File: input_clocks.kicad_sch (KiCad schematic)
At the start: 86 parts, among them J201 REFIN, J202 REFIN_DIRECT_P, J203 REFIN_DIRECT_N, J208 VTUNE, T201 TC2-1T+, U203 TSV914, U204 74LVC1G66, X201 XTCLH40M000CHJA0P0

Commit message: Updated schematics
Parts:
- removed J?: TCXO_ON_LED, symbol Connector_Generic:Conn_01x02
- added D?: TCXO_ON, LED_SMD:LED_0603_1608Metric_Pad1.05x0.95mm_HandSolder, symbol Device:LED
- added FB?: TODO, Inductor_SMD:L_0603_1608Metric_Pad1.05x0.95mm_HandSolder, symbol Device:FerriteBead_Small
- added R? (x2): DNP, Resistor_SMD:R_0603_1608Metric_Pad0.98x0.95mm_HandSolder, symbol Device:R
- added R?: TODO, Resistor_SMD:R_0603_1608Metric_Pad0.98x0.95mm_HandSolder, symbol Device:R
- R?: value 470 -> 2k
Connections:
- net +5V: now also FB?.1; no longer C?.1, U?.2 (VIN)
- net CLKIN_0: now also R?.1
- net DUTY_OUT_N: now also D207.1 (K), D208.2 (A), R?.2
- net DUTY_OUT_P: now also R227.1, R?.2
- net GND: now also C?.1, R?.2; no longer C?.2
- net VCC_TCXO: now also D?.2 (A); no longer R?.2
- net Vctrl: now also R?.2; no longer C227.1, D?.3, J208.1 (In)
- net ~{CLKIN_0}: now also R?.1
- net at R?.1: now also D?.1 (K)
- net at D207.2 (A), D208.1 (K): now also R227.2
- new net: C227.1, D?.3, J208.1 (In), R?.1
- new net: C?.2, FB?.2, U?.2 (VIN)
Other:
- moved on the sheet: C205, C206, C216, C217, C218, C225, C226, C227, C228, C230, C232, C234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

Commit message: Finished schematics
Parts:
- added JP503: Jumper_2_Bridged, symbol Jumper:Jumper_2_Bridged
- gave numbers to parts that had none: 19
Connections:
- net VCC renamed VCC_fREF
- net VCC_fREF: now also JP503.1 (A); no longer U204.5 (VCC)
- new net: JP503.2 (B), U204.5
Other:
- company: (none) -> Petr Polasek
- title: (none) -> Generator 0.0125 - 6.4 GHz (0.02 - 9.8 GHz)
- moved on the sheet: C225, C226, C228, C232, C235, C501, C503, D207, D208, R227, R230, R231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

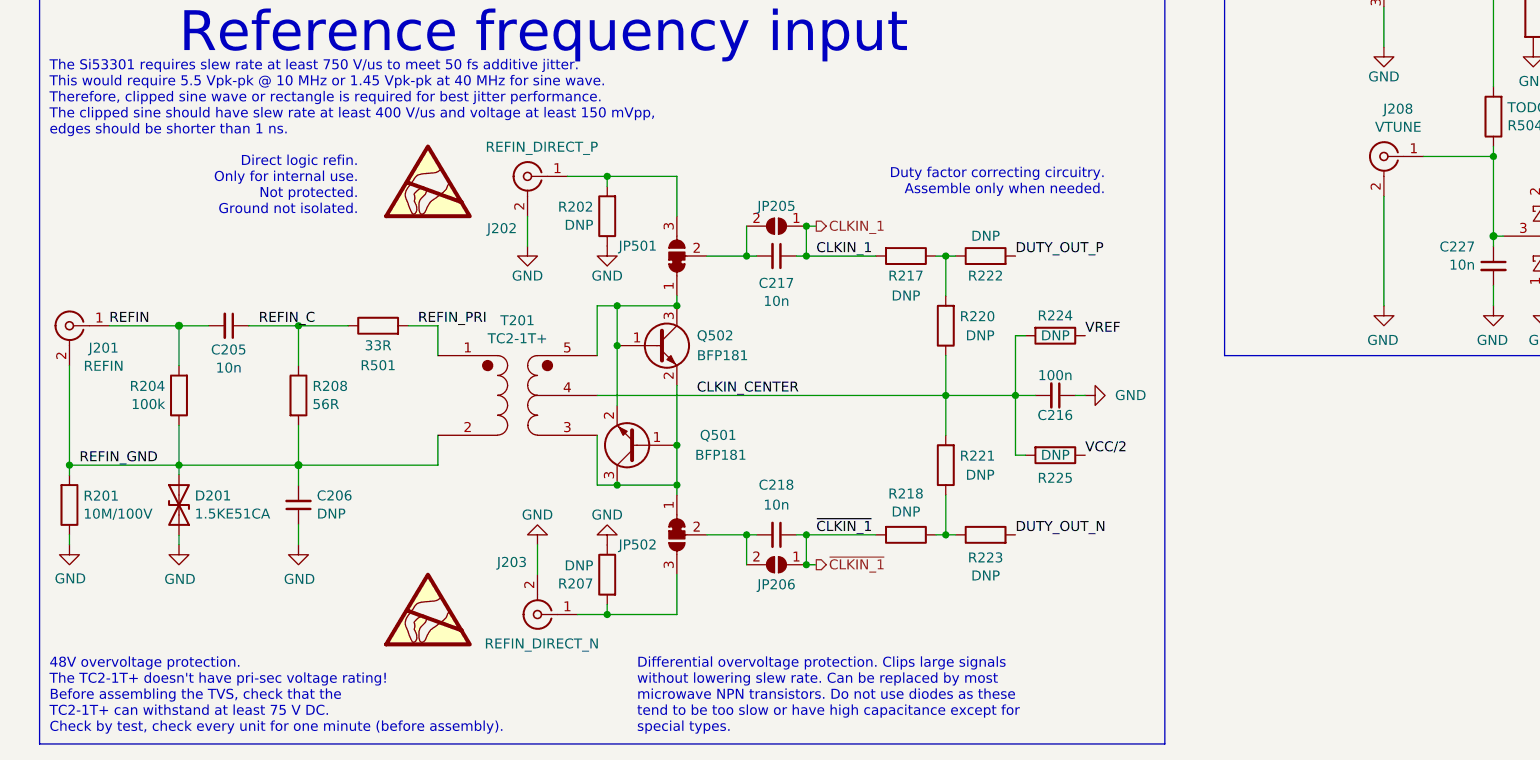
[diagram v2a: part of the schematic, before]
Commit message: Schematic fixes
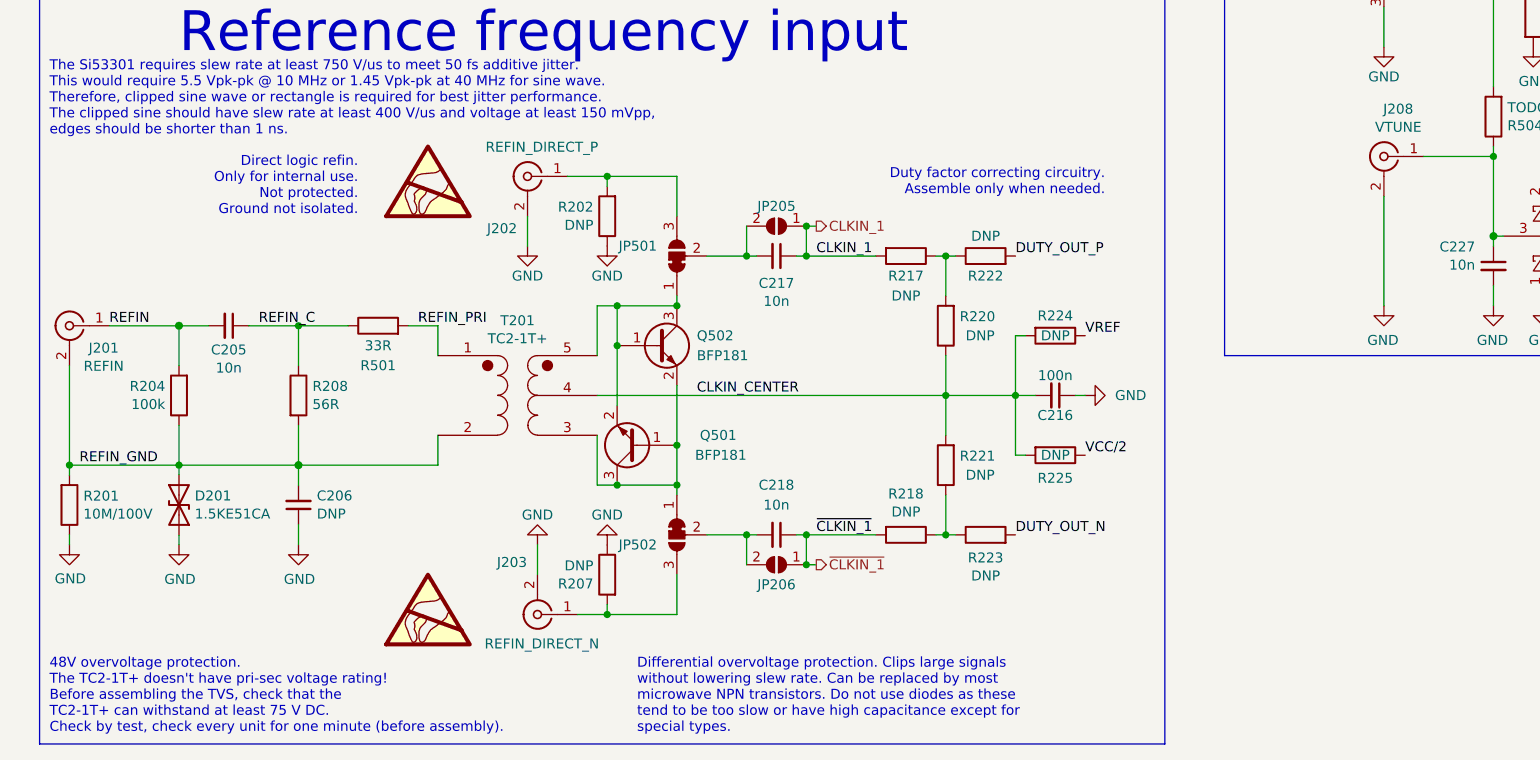
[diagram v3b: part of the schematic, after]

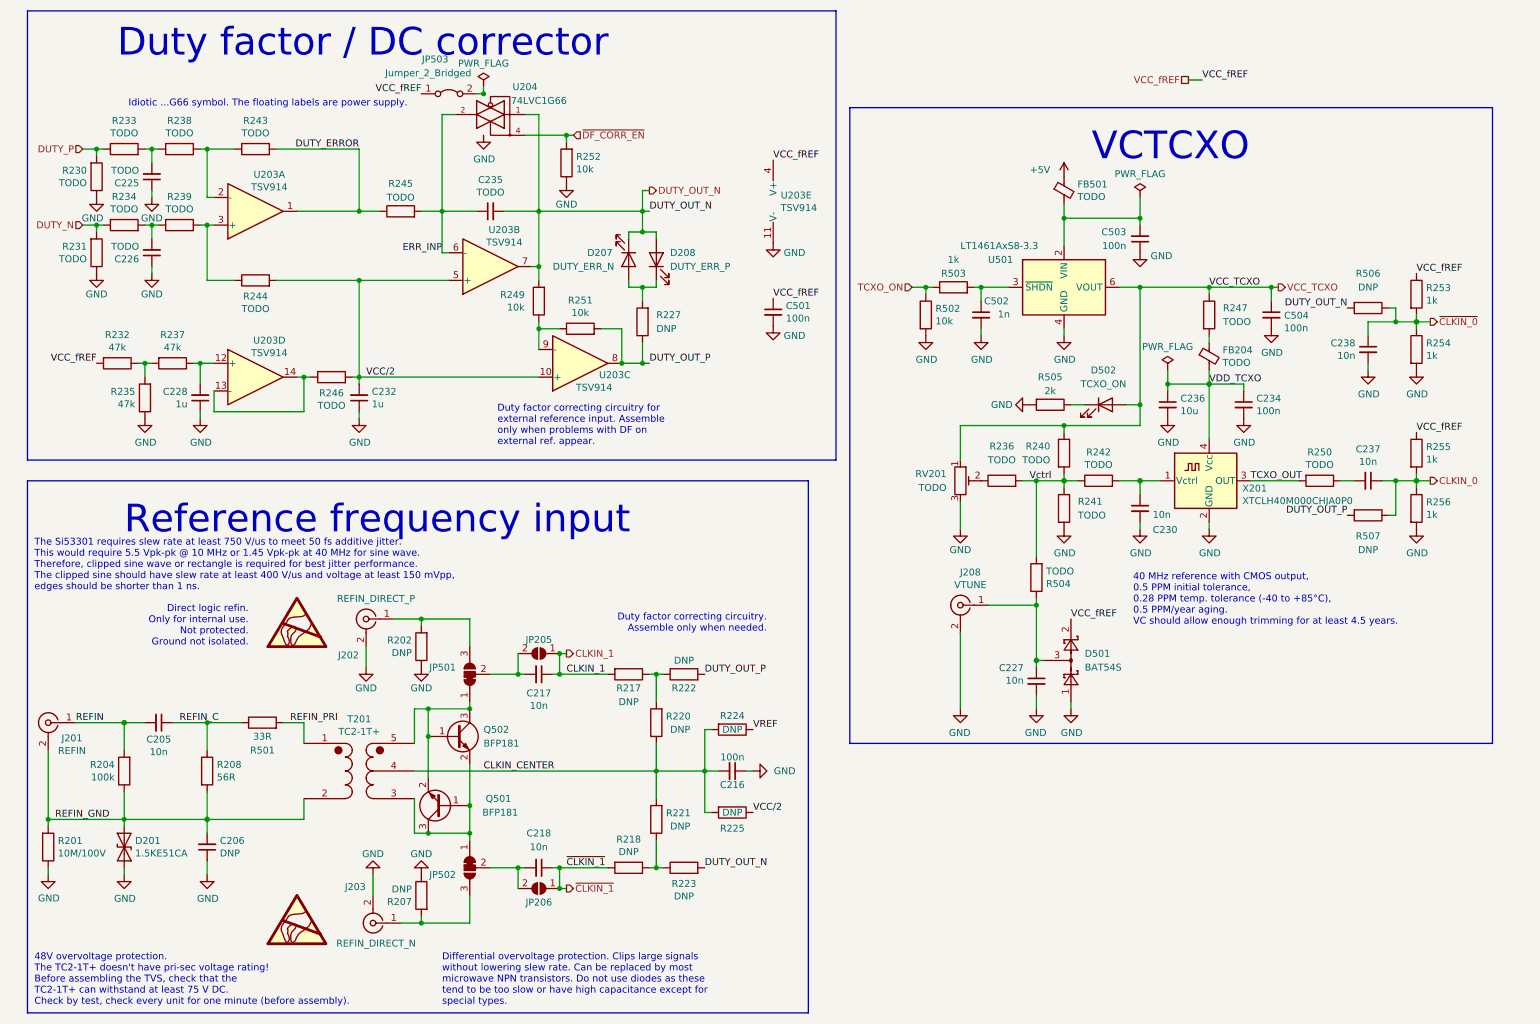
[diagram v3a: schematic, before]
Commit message: Schematic checked. All footprints assigned. Electrolytics need footprint check, so do the RS485 and power connectors and the MuRata oscillator (also it is now EOL) and the crystal. The power protection transils on aux input/output need replacement. PCB in sync with SCH.
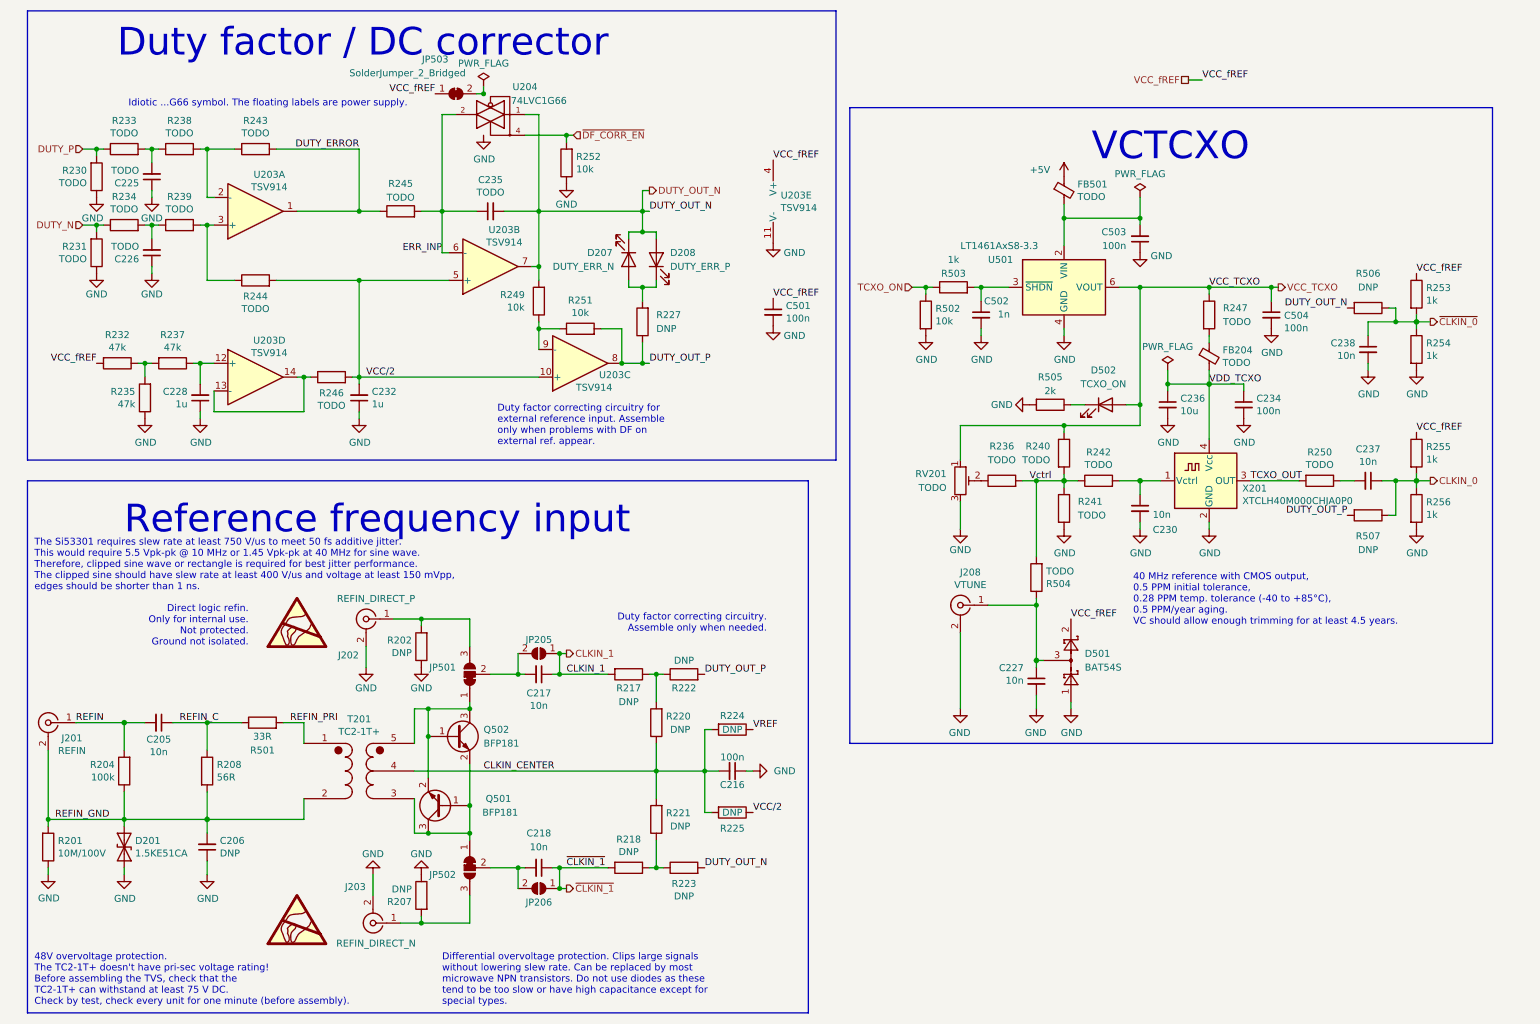
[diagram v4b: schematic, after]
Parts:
- removed JP503: Jumper_2_Bridged, symbol Jumper:Jumper_2_Bridged
- added JP503: SolderJumper_2_Bridged, Jumper:SolderJumper-2_P1.3mm_Bridged_RoundedPad1.0x1.5mm, symbol Jumper:SolderJumper_2_Bridged
- J202, J203, J208: footprint petr_kicad:SMA_rosenberger_hybrid -> Connector_Coaxial:U.FL_Molex_MCRF_73412-0110_Vertical
- JP501, JP502: footprint (none) -> Jumper:SolderJumper-3_P1.3mm_Bridged12_RoundedPad1.0x1.5mm_NumberLabels
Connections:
- net VCC_fREF: now also JP503.1 (A)
- net at U204.5: now also JP503.2 (B)

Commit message: Resolved all broken symbols / packages / links except TCXO.
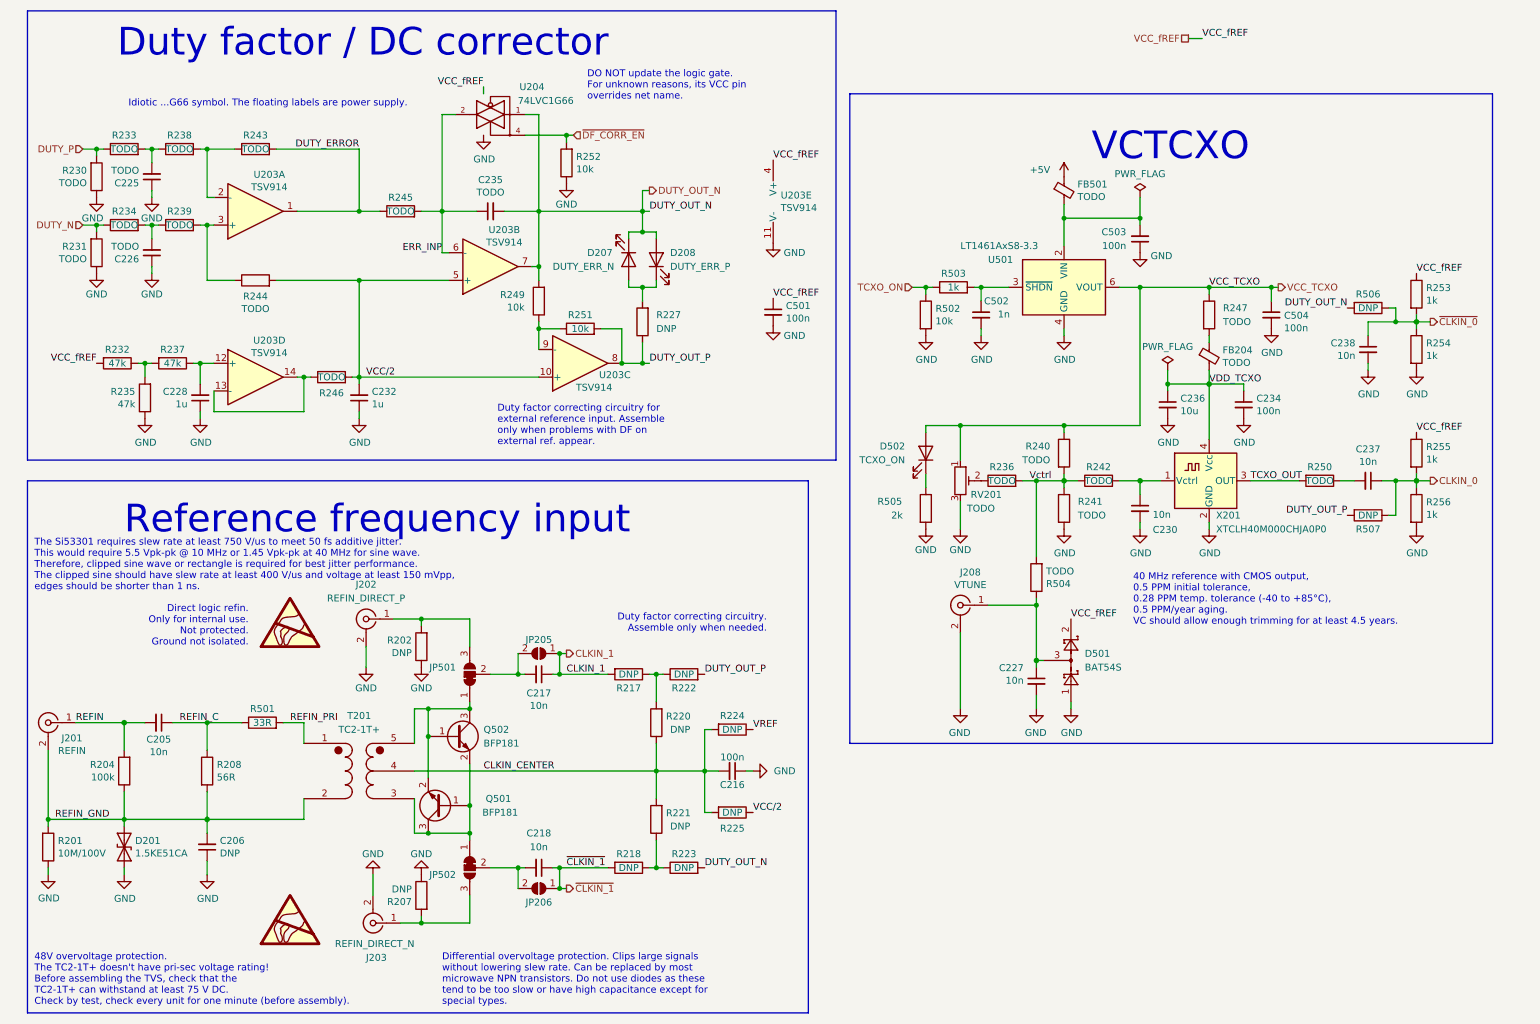
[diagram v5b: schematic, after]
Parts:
- removed J202: REFIN_DIRECT_P, Connector_Coaxial:U.FL_Molex_MCRF_73412-0110_Vertical, symbol Connector:Conn_Coaxial
- removed J203: REFIN_DIRECT_N, Connector_Coaxial:U.FL_Molex_MCRF_73412-0110_Vertical, symbol Connector:Conn_Coaxial
- removed JP503: SolderJumper_2_Bridged, Jumper:SolderJumper-2_P1.3mm_Bridged_RoundedPad1.0x1.5mm, symbol Jumper:SolderJumper_2_Bridged
- removed T201: TC2-1T+, Transformer_SMD:Transformer_MACOM_SM-22, symbol petr_lib_nightly:TC2-1T+
- added J202: REFIN_DIRECT_P, Connector_Coaxial:U.FL_Molex_MCRF_73412-0110_Vertical, symbol petr:u.FL
- added J203: REFIN_DIRECT_N, Connector_Coaxial:U.FL_Molex_MCRF_73412-0110_Vertical, symbol petr:u.FL
- added T201: TC2-1T+, petr:Transformer_MiniCircuits_AT224-1A, symbol petr:TC2-1T+
- J201: symbol Connector:Conn_Coaxial -> petr:SMA_Rosenberger_32K243-40ML5_chinese_SMA_hybrid
- J208: symbol Connector:Conn_Coaxial -> petr:u.FL
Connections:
- net CLKIN_CENTER: now also T201.4 (SC)
- net GND: now also J202.2 (Ext), J203.2 (Ext)
- net REFIN_GND: now also T201.2 (AB)
- net REFIN_PRI: now also T201.1 (AA)
- net VCC_fREF: now also U204.5 (VCC_fREF)
- net at JP501.1 (A), Q501.2 (E), Q502.1 (B)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: now also T201.5 (SB)
- net at JP502.1 (A), Q501.1 (B), Q501.3 (C)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: now also T201.3 (SA)
- net at JP502.3 (B), R207.2: now also J203.1 (In)
- net at JP501.3 (B), R202.2: now also J202.1 (In)
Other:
- note added: "DO NOT update the logic gate. For unknown reasons, its VCC pin overrides net name."
- moved on the sheet: D502, R505
